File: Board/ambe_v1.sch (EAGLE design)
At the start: 49 parts, among them IC3 AMBE-3000LQFP-128

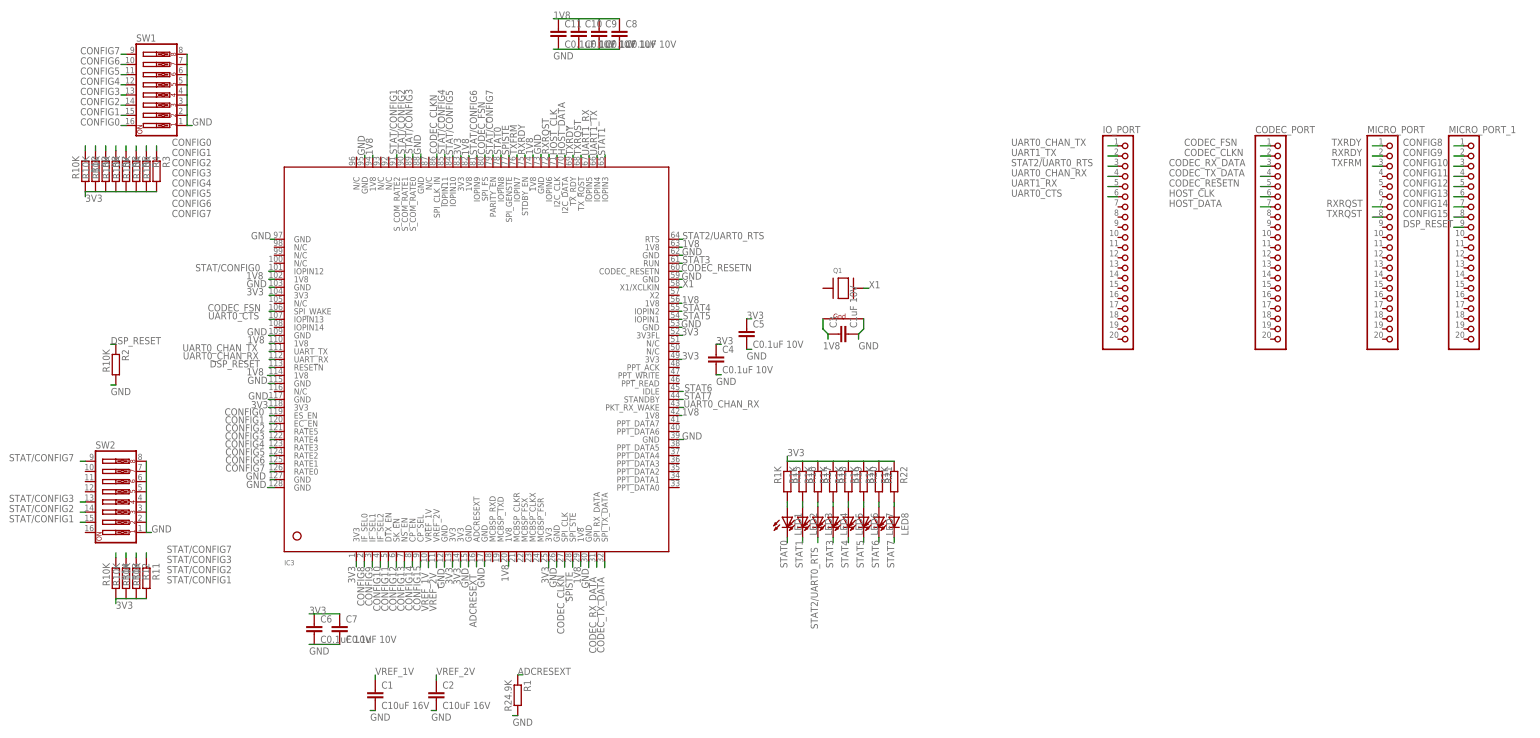
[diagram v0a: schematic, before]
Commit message: Progress on routing board
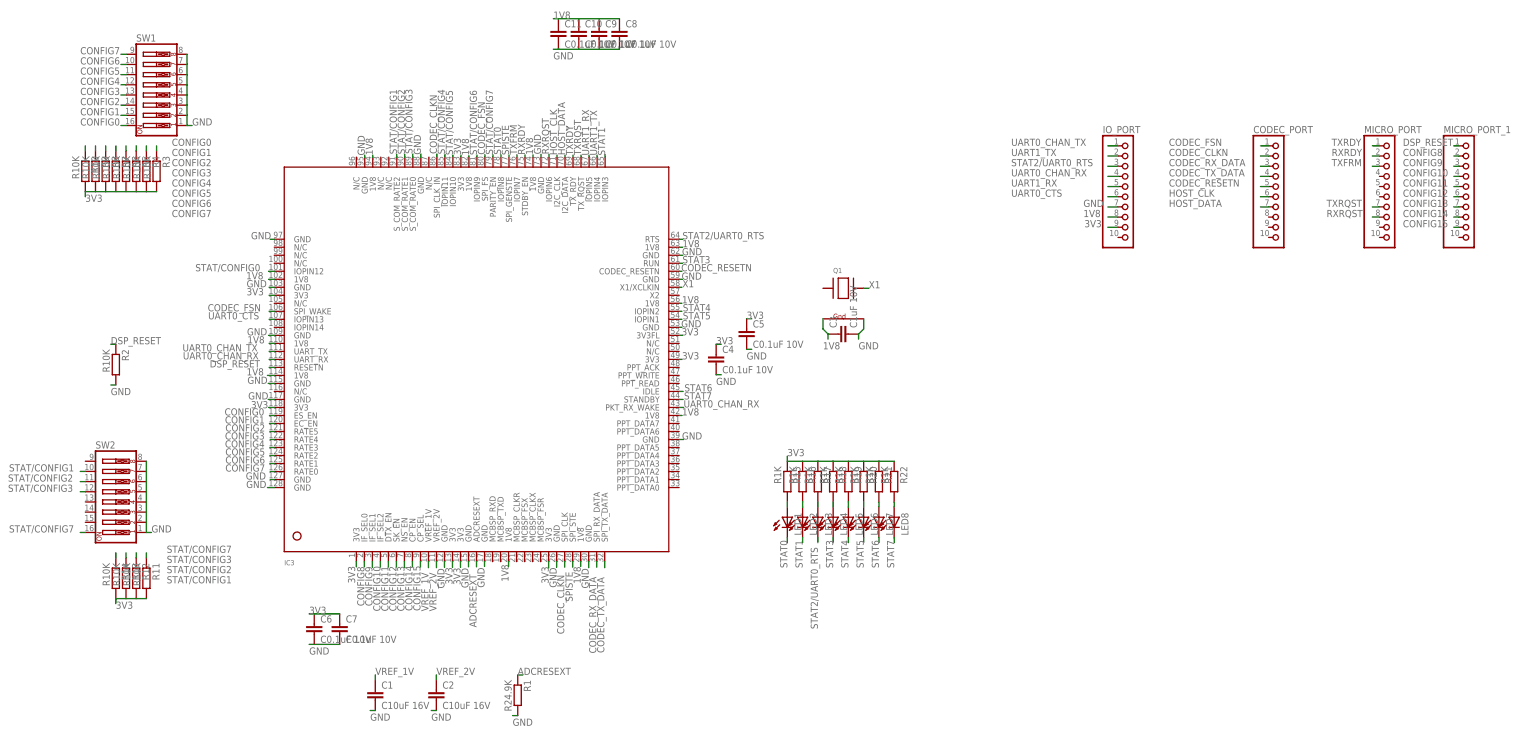
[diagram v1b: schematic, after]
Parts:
- CODEC_PORT, IO_PORT, MICRO_PORT, MICRO_PORT_1: device pinhead:PINHD-1X20 -> pinhead:PINHD-1X10
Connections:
- net 1V8: now also IO_PORT.8
- net 3V3: now also IO_PORT.9
- net CONFIG10: now also MICRO_PORT_1.4; no longer MICRO_PORT_1.3
- net CONFIG11: now also MICRO_PORT_1.5; no longer MICRO_PORT_1.4
- net CONFIG12: now also MICRO_PORT_1.6; no longer MICRO_PORT_1.5
- net CONFIG13: now also MICRO_PORT_1.7; no longer MICRO_PORT_1.6
- net CONFIG14: now also MICRO_PORT_1.8; no longer MICRO_PORT_1.7
- net CONFIG15: now also MICRO_PORT_1.9; no longer MICRO_PORT_1.8
- net CONFIG8: now also MICRO_PORT_1.2; no longer MICRO_PORT_1.1
- net CONFIG9: now also MICRO_PORT_1.3; no longer MICRO_PORT_1.2
- net DSP_RESET: now also MICRO_PORT_1.1; no longer MICRO_PORT_1.9
- net GND: now also IO_PORT.7
- net RXRQST: now also MICRO_PORT.8; no longer MICRO_PORT.7
- net STAT/CONFIG1: now also SW2.10; no longer SW2.15
- net STAT/CONFIG2: now also SW2.11; no longer SW2.14
- net STAT/CONFIG3: now also SW2.12; no longer SW2.13
- net STAT/CONFIG7: now also SW2.16; no longer SW2.9
- net TXRQST: now also MICRO_PORT.7; no longer MICRO_PORT.8

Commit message: Finish routing ambe board
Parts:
- removed LED1, LED2, LED3, LED4, LED5, LED6, LED7, LED8: (no value), SparkFun-LED:LED0603
- removed R15, R16, R17, R18, R19, R20, R21, R22: R1K, resistor:R-EU_R0805
- MICRO_PORT: device pinhead:PINHD-1X10 -> pinhead:PINHD-1X5
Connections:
- removed net N$1: LED1.A, R15.2
- removed net N$2: LED2.A, R16.2
- removed net N$3: LED3.A, R17.2
- removed net N$4: LED4.A, R18.2
- removed net N$5: LED5.A, R19.2
- removed net N$6: LED6.A, R20.2
- removed net N$7: LED7.A, R21.2
- removed net N$8: LED8.A, R22.2
- net 3V3: no longer R15.1, R16.1, R17.1, R18.1, R19.1, R20.1, R21.1, R22.1
- net CODEC_CLKN: now also CODEC_PORT.1; no longer CODEC_PORT.2
- net CODEC_FSN: now also CODEC_PORT.7; no longer CODEC_PORT.1
- net CODEC_RESETN: now also CODEC_PORT.4; no longer CODEC_PORT.5
- net CODEC_RX_DATA: now also CODEC_PORT.2; no longer CODEC_PORT.3
- net CODEC_TX_DATA: now also CODEC_PORT.3; no longer CODEC_PORT.4
- net HOST_DATA: now also CODEC_PORT.5; no longer CODEC_PORT.7
- net RXRDY: now also MICRO_PORT.4; no longer MICRO_PORT.2
- net RXRQST: now also MICRO_PORT.3; no longer MICRO_PORT.8
- net STAT0: no longer LED1.C
- net STAT1: no longer LED2.C
- net STAT2/UART0_RTS: now also IO_PORT.4; no longer IO_PORT.3, LED3.C
- net STAT3: no longer LED4.C
- net STAT4: no longer LED5.C
- net STAT5: no longer LED6.C
- net STAT6: no longer LED7.C
- net STAT7: no longer LED8.C
- net TXFRM: now also MICRO_PORT.5; no longer MICRO_PORT.3
- net TXRDY: now also MICRO_PORT.2; no longer MICRO_PORT.1
- net TXRQST: now also MICRO_PORT.1; no longer MICRO_PORT.7
- net UART0_CHAN_RX: now also IO_PORT.1; no longer IO_PORT.4
- net UART0_CHAN_TX: now also IO_PORT.2; no longer IO_PORT.1
- net UART0_CTS: now also IO_PORT.3; no longer IO_PORT.6
- net UART1_RX: now also IO_PORT.6; no longer IO_PORT.5
- net UART1_TX: now also IO_PORT.5; no longer IO_PORT.2

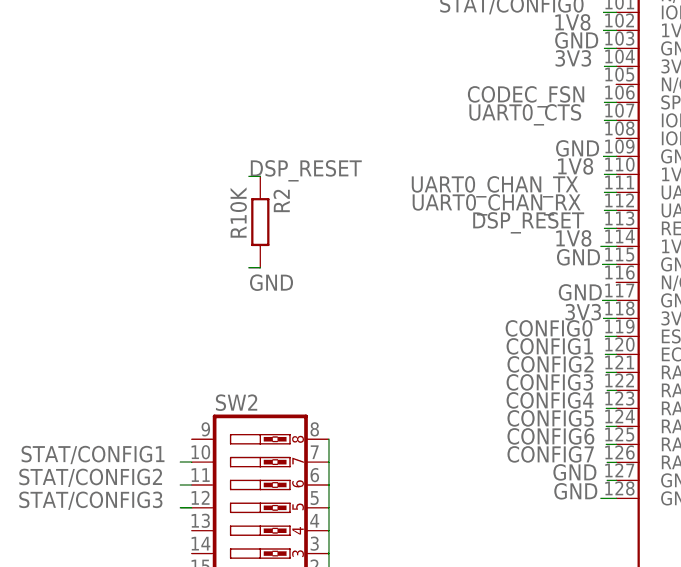
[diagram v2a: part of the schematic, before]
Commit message: + pull up to AMBE's Reset & progress in ModemIO brd
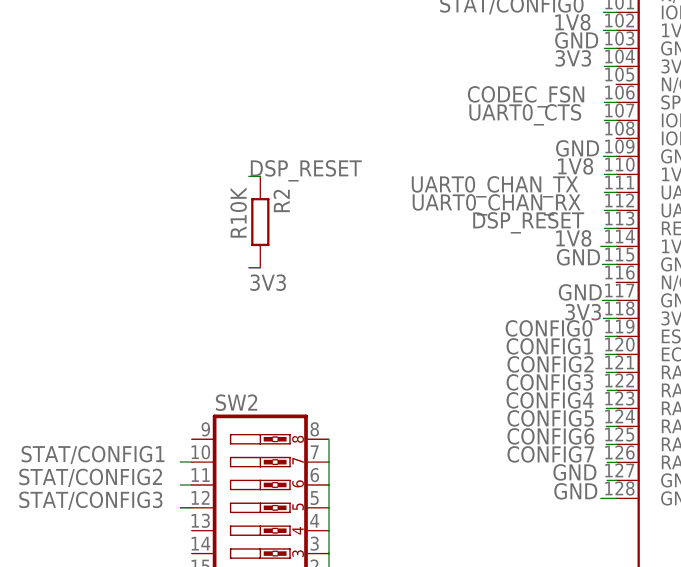
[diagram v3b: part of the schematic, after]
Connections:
- net 3V3: now also R2.2
- net GND: no longer R2.2
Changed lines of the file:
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@@
 <setting verticaltext="up"/>
 </settings>
-<grid distance="0.01" unitdist="inch" unit="inch" style="lines" multiple="1" display="no" altdistance="0.01" altunitdist="inch" altunit="inch"/>
+<grid distance="0.1" unitdist="inch" unit="inch" style="lines" multiple="1" display="no" altdistance="0.01" altunitdist="inch" altunit="inch"/>
 <layers>
 <layer number="1" name="Top" color="4" fill="1" visible="no" active="no"/>
@@
 <label x="378.968" y="275.59" size="1.778" layer="95"/>
 </segment>
+<segment>
+<pinref part="R2" gate="G$1" pin="2"/>
+<wire x1="137.16" y1="236.22" x2="135.89" y2="236.22" width="0.1524" layer="91"/>
+<label x="135.89" y="233.68" size="1.778" layer="95"/>
+</segment>
 </net>
 <net name="VREF_1V" class="0">
@@
 </segment>
 <segment>
-<pinref part="R2" gate="G$1" pin="2"/>
-<wire x1="137.16" y1="236.22" x2="135.89" y2="236.22" width="0.1524" layer="91"/>
-<label x="135.89" y="233.68" size="1.778" layer="95"/>
-</segment>
-<segment>
